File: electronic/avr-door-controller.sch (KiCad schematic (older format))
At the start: 74 parts, among them CON1 24V, J1 DOOR1, J2 DOOR2, P1 Digital, P10 DOOR2 BTN, P2 Analog, P3 DOOR1 BTN, P6 USB_A, P7 CLOCK, Q1 Q_NPN_EBC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

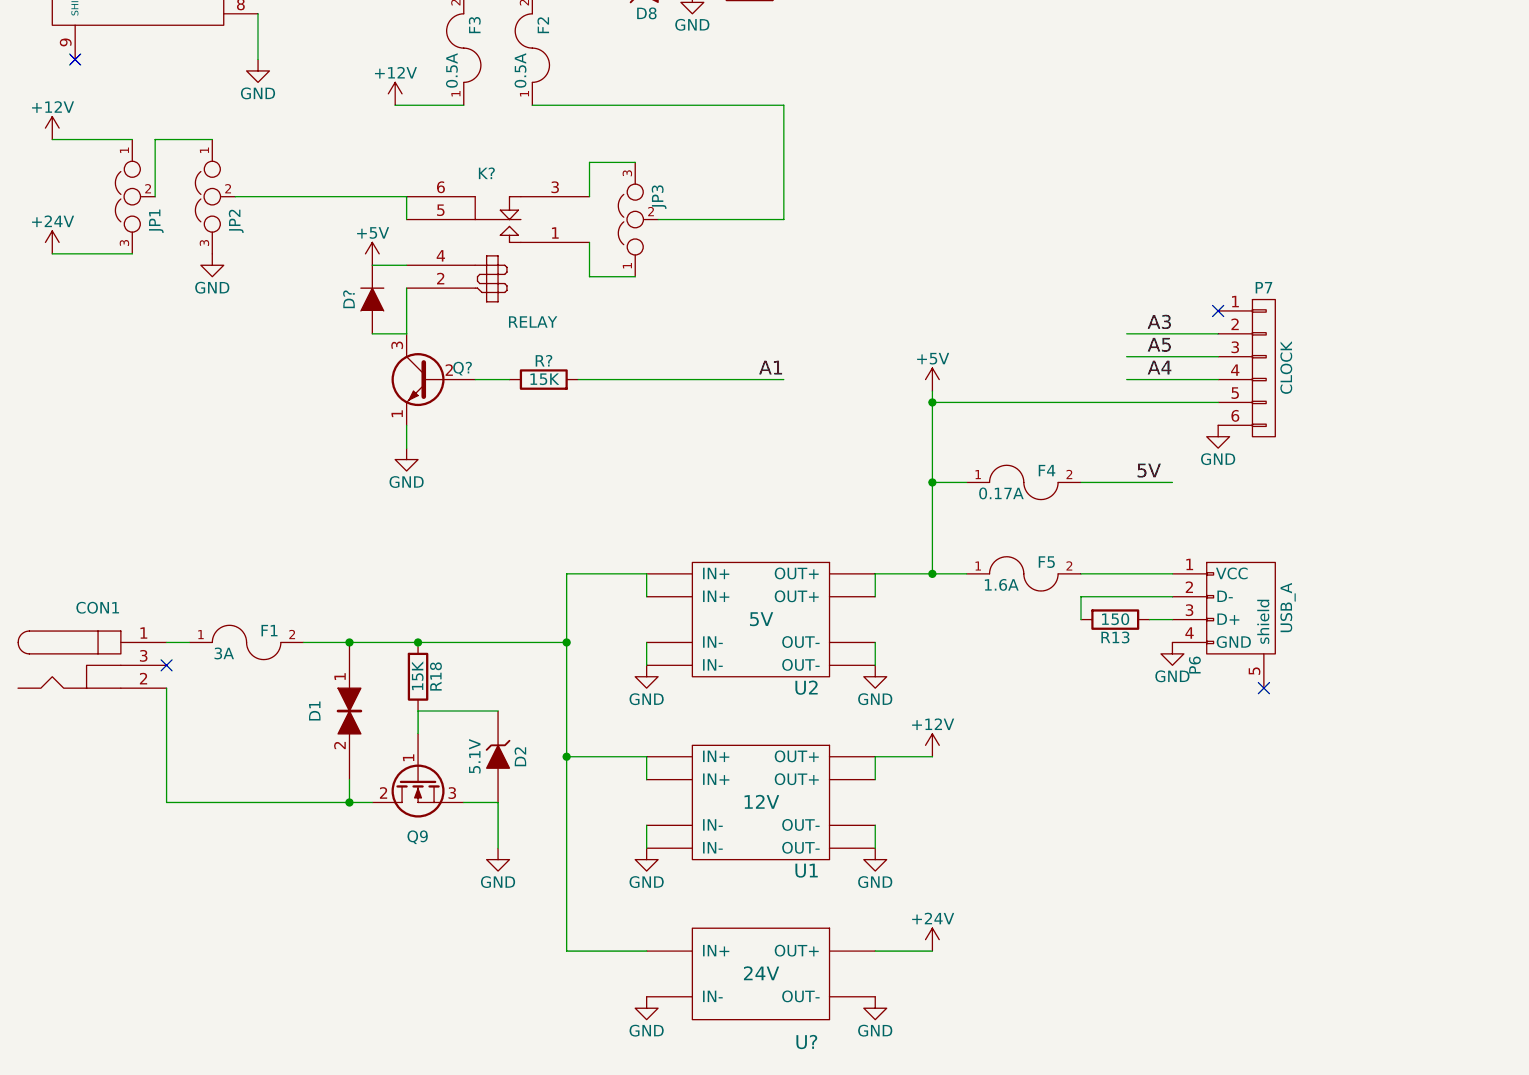
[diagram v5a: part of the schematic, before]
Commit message: electronic: schematics: Move the power input back on the sheet
Signed-off-by: Alban Bedel <albeu@free.fr>
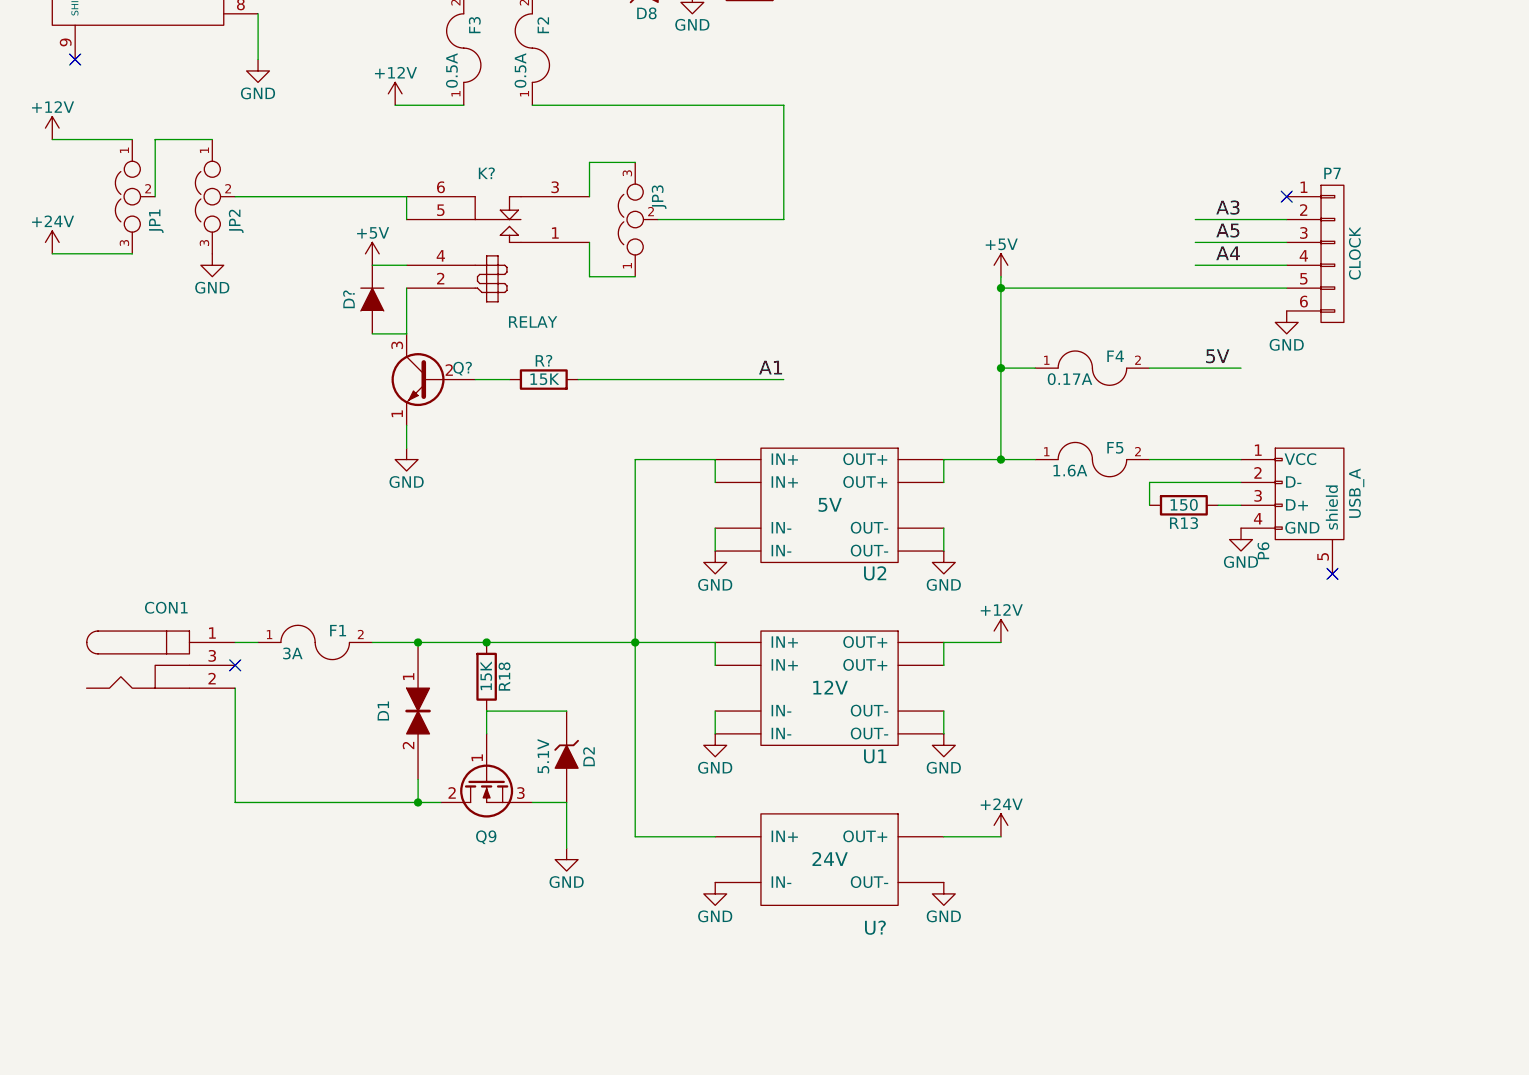
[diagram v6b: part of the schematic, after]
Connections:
- wire segments 210 -> 209
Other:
- moved on the sheet: CON1, D1, D2, F1, F4, F5, P6, P7, Q9, R13, R18, U1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

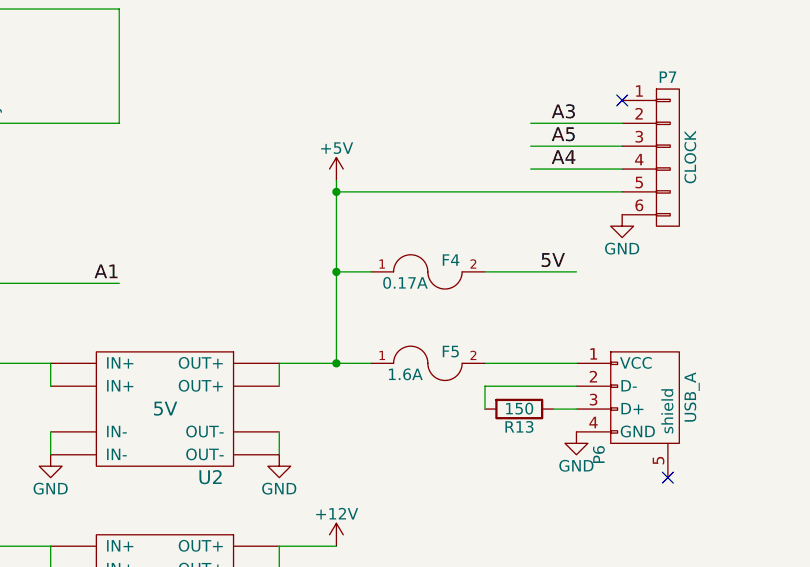
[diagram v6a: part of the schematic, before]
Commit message: electronic: schematics: Change the arduino fuse to 90mA
90mA is enough and should really trip before the Arduino take too much
damage.

Signed-off-by: Alban Bedel <albeu@free.fr>
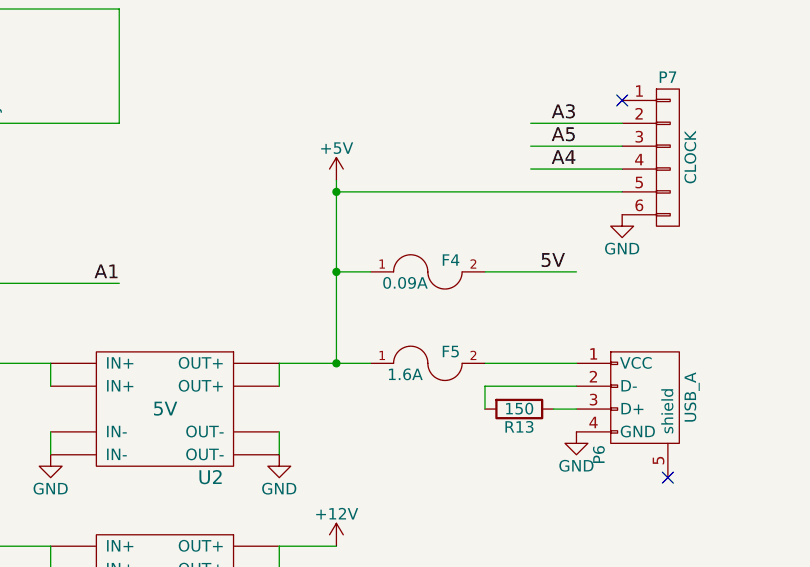
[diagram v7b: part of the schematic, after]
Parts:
- F4: value 0.17A -> 0.09A
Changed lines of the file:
@@
 P 5350 5250
 F 0 "F4" H 5450 5300 50  0000 C CNN
-F 1 "0.17A" H 5250 5200 50  0000 C CNN
+F 1 "0.09A" H 5250 5200 50  0000 C CNN
 F 2 "PPTC:Bourns_PPTC_Style_1" H 5350 5250 50  0001 C CNN
 F 3 "" H 5350 5250 50  0000 C CNN
